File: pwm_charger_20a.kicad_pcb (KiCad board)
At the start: 2 copper layers, 90 x 85 mm, 127 parts, among them J1 MKDS 5/ 2-9,5, J2 MKDS 5/ 2-9,5, J3 MKDS 5/ 2-9,5, J4 UEXT, J5 USB_A, J6 PWR_12V, J7 6P6C, J8 ST_Nucleo_SWD_5p, Q1 PSMN7R5-60YLX, Q2 PSMN7R5-60YLX, Q3 PSMN7R5-60YLX, Q6 IRFB7787, Q7 IRFB7787, Q8 IRFB7787, T1 MMBT3904, T2 MMBT3906, T3 MMBT3904, T4 MMBT3904, T5 MMBT3904, U1 STM32L072CZTx, U2 TLV9002, U3 MC34063AD, U4 D1213A-04SO, U5 LP2950-3.3_TO252

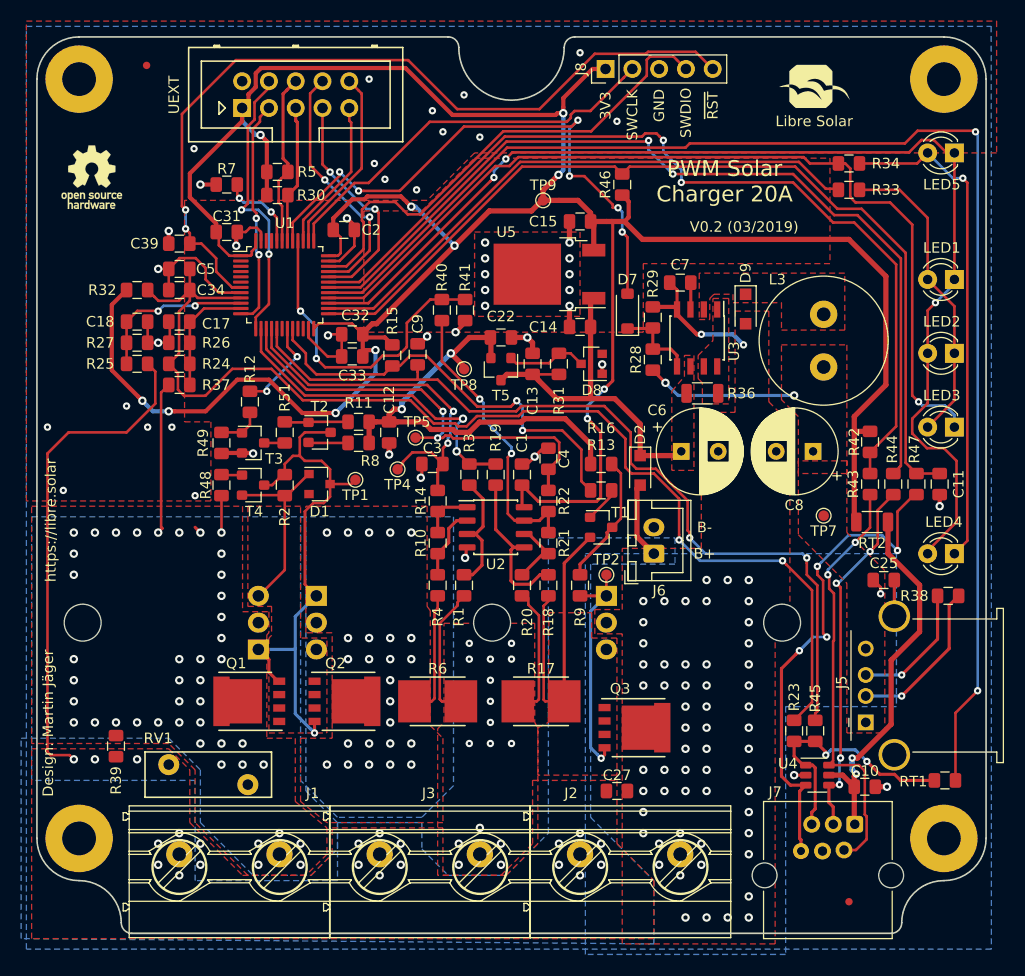
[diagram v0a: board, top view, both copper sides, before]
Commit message: Updates after manufacturer feedback
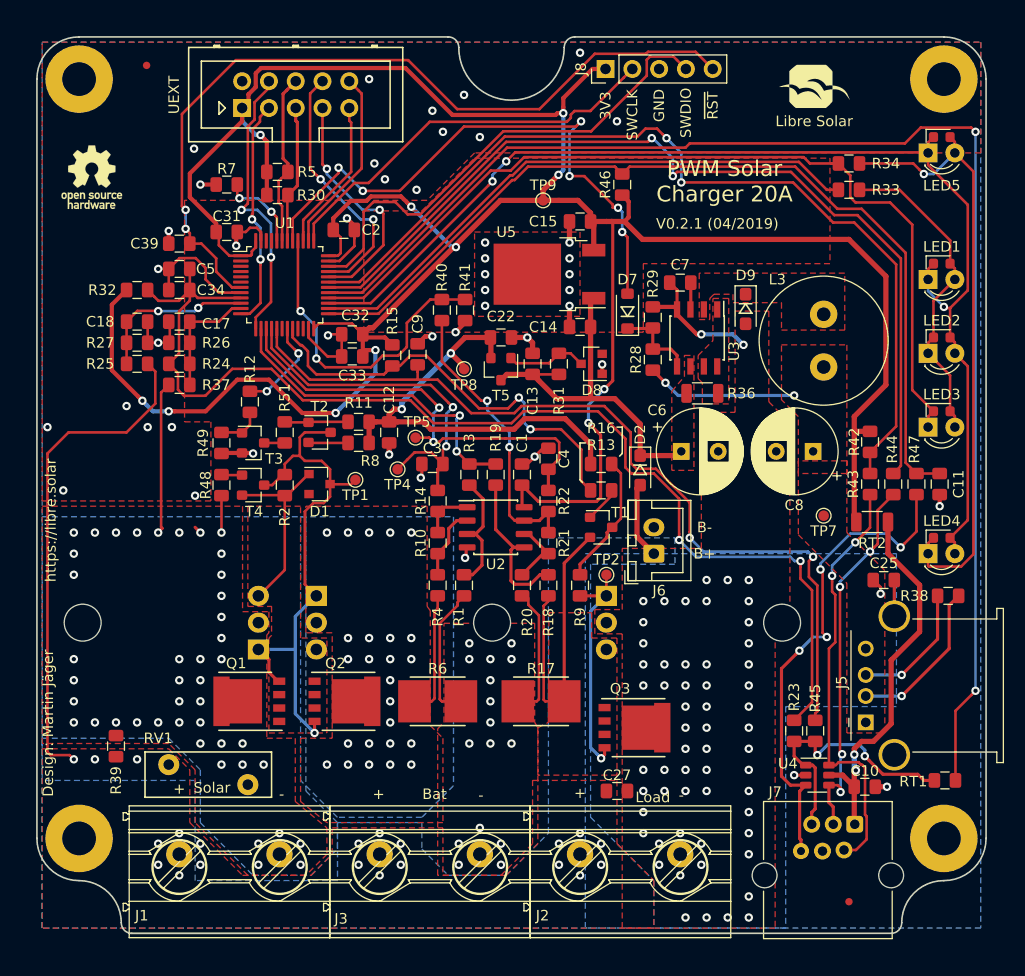
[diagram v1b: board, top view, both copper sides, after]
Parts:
- D2, D9: footprint Diode_SMD:D_SOD-123F -> LibreSolar:D_SOD-123F
- LED1, LED2, LED3, LED4, LED5: footprint LED_THT:LED_D3.0mm -> LibreSolar:LED_0603_D3.0mm
- moved LED1 1.92 mm to (184.3, 74.5), turned to 0 degrees
- moved LED2 1.92 mm to (184.3, 81.5), turned to 0 degrees
- moved LED3 1.92 mm to (184.3, 88.5), turned to 0 degrees
- moved LED4 1.92 mm to (184.3, 100.5), turned to 0 degrees
- moved LED5 1.92 mm to (184.3, 62.5), turned to 0 degrees
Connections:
- net Net-(J7-Pad2) renamed /MCU/RX
- net Net-(J7-Pad3) renamed /MCU/TX
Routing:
- net Net-(LED4-Pad1): track 47.5 -> 58.4 mm
- net /MCU/LED_C: track 87.2 -> 85.0 mm, vias 1 -> 0
- net /MCU/LED_B: track 110.1 -> 112.2 mm
- net /MCU/TEMP_EXT: track 24.8 -> 26.0 mm
- net Net-(LED1-Pad2): track 29.5 -> 30.6 mm
- net /MCU/USART1_TX: track 85.9 -> 86.9 mm
- net /MCU/TX: track 35.0 -> 35.9 mm
- net T_BAT: track 81.6 -> 82.5 mm
- net USB_PWR_DIS: track 54.7 -> 55.6 mm
- net /MCU/SPI1_MISO: track 21.9 -> 22.8 mm
- net VDDA: track 110.9 -> 111.6 mm
- net /MCU/USART1_RX: track 87.0 -> 87.7 mm
- net /MCU/SPI1_MOSI: track 24.0 -> 24.6 mm
- net Net-(J7-Pad6): track 47.6 -> 47.1 mm
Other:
- net class Default: via_dia 0.7 -> 0.8; via_drill 0.3 -> 0.4
- rule trace_min: 0.2 -> 0.25
- rule via_min_drill: 0.3 -> 0.4
- rule via_min_size: 0.3 -> 0.7
- board text added: "V0.2.1 (04/2019)"
- board text removed: "V0.2 (03/2019)"
